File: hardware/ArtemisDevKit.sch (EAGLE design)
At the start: 77 parts, among them J1 USB, J10 SMD, J11 SMD, J12 PTH, J14 PTH, J2 CORTEX_JTAG_DEBUG_MINIMUM_PTH, J22 PTH, J23 PTH, J24 PTH, J25 PTH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

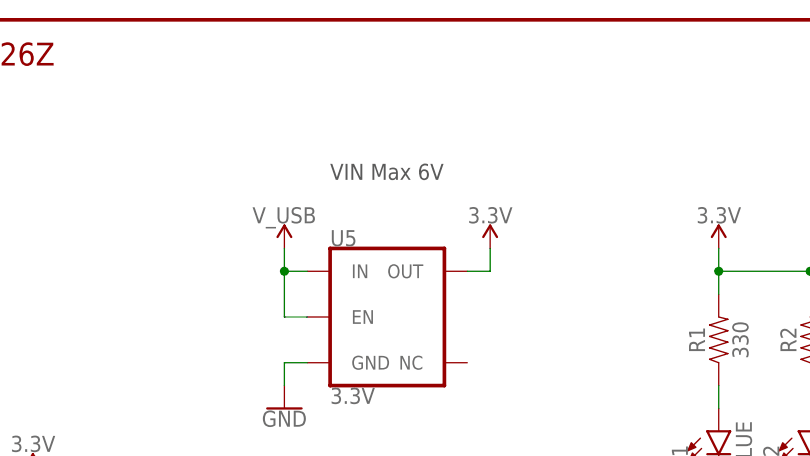
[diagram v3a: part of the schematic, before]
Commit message: remove VIN maximum
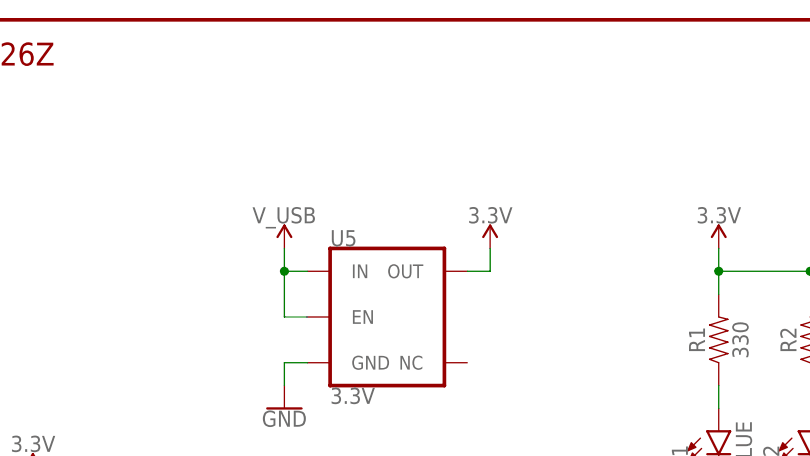
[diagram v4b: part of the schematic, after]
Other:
- note removed: "VIN Max 6V"
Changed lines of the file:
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@@
 clock  from interface chip</text>
 <text x="363.22" y="180.34" size="1.778" layer="97" font="vector">power rail intended for output only</text>
-<text x="71.12" y="261.62" size="1.778" layer="97">VIN Max 6V</text>
 </plain>
 <instances>

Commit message: replace 8+4 smd headers with 12
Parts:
- removed J10, J11: SMD, SparkFun-Connectors:CONN_08SMD-COMBO-FEMALE
- J5, J9: value 1X04_SMD_STRAIGHT_COMBO -> (none); device SparkFun-Connectors:CONN_04SMD_STRAIGHT_COMBO -> SparkFun-Connectors:CONN_12SMD_COMBINED
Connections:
- net D13: now also J9.5; no longer J11.1
- net D16: now also J5.12; no longer J5.4
- net D25: now also J9.11; no longer J11.7
- net D26: now also J9.10; no longer J11.6
- net D28: now also J9.12; no longer J11.8
- net D29: now also J9.8; no longer J11.4
- net D31: now also J5.11; no longer J5.3
- net D32: now also J9.7; no longer J11.3
- net D33: now also J9.6; no longer J11.2
- net D34: now also J9.9; no longer J11.5
- net D36: now also J5.6; no longer J10.6
- net D37: now also J5.4; no longer J10.4
- net D38: now also J5.5; no longer J10.5
- net D39: now also J5.1; no longer J10.1
- net D40: now also J5.2; no longer J10.2
- net D41: now also J5.10; no longer J5.2
- net D42: now also J5.7; no longer J10.7
- net D43: now also J5.8; no longer J10.8
- net D44: now also J5.3; no longer J10.3
- net D45: now also J5.9; no longer J5.1
